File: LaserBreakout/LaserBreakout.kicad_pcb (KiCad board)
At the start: 2 copper layers, 55.9 x 34.3 mm, 7 parts, among them J1 LASER_CONN, J2 949, J3 MiniFitPower

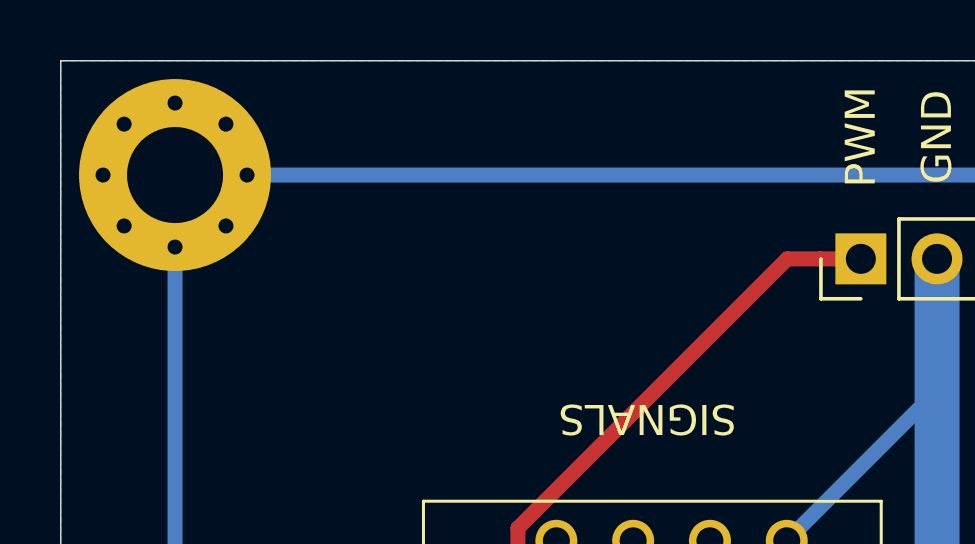
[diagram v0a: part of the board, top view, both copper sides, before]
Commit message: Add more breakout boards
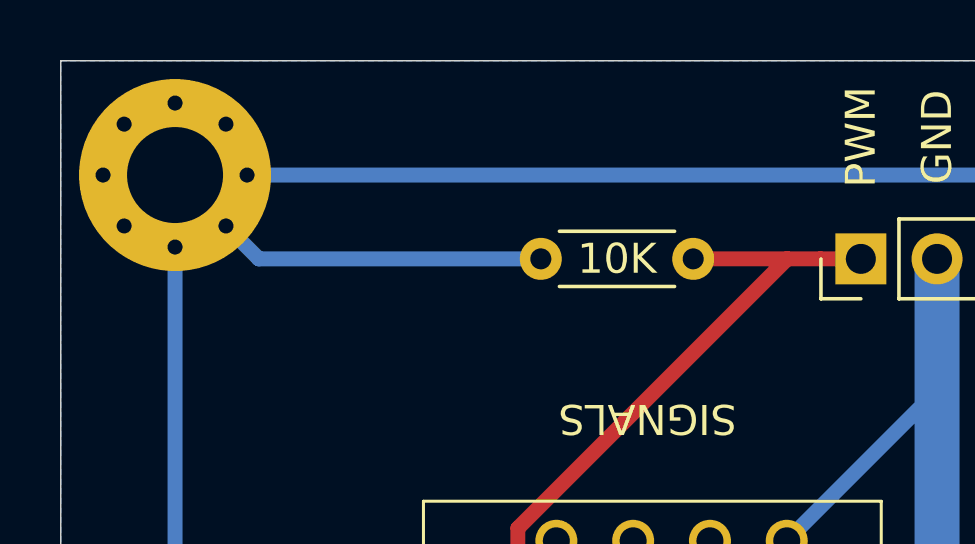
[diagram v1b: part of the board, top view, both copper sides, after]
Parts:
- added R1: 10K, Resistor_THT:R_Axial_DIN0204_L3.6mm_D1.6mm_P5.08mm_Horizontal, F.Cu at (106.2, 77.7)
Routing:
- net GND: track 204.1 -> 217.4 mm
- net 1: track 18.1 -> 21.2 mm
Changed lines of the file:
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@@
     (thickness 1.6)
     (drawings 16)
-    (tracks 21)
+    (tracks 24)
     (zones 0)
-    (modules 7)
+    (modules 8)
     (nets 12)
   )
@@
   (layers
     (0 F.Cu signal)
-    (31 B.Cu signal hide)
+    (31 B.Cu signal)
     (32 B.Adhes user)
     (33 F.Adhes user)
@@
   )
   (setup
-    (last_trace_width 1.5)
+    (last_trace_width 0.5)
     (user_trace_width 0.5)
     (user_trace_width 1)
@@
     (solder_mask_min_width 0.25)
     (aux_axis_origin 0 0)
-    (visible_elements 7FFFFFFF)
+    (visible_elements 7FFFFF7F)
     (pcbplotparams
       (layerselection 0x010fc_ffffffff)
@@
     (pad 9 thru_hole circle (at -1.235 6.35 90) (size 1.625 1.625) (drill 3.25) (layers *.Cu *.Mask F.SilkS))
     (pad 10 thru_hole circle (at 10.195 6.35 90) (size 1.625 1.625) (drill 3.25) (layers *.Cu *.Mask F.SilkS))
+    (model ${KIPRJMOD}/../libs/Keystone949/949.stp
+      (at (xyz 0 0 0))
+      (scale (xyz 1 1 1))
+      (rotate (xyz 0 0 0))
+    )
   )
   (module Connector_Molex:Molex_Mini-Fit_Jr_5566-04A_2x02_P4.20mm_Vertical (layer F.Cu)
@@
     (pad 4 thru_hole oval (at 4.2 5.5 180) (size 2.7 3.3) (drill 1.4) (layers *.Cu *.Mask)
       (net 5 24V))
-    (model ${KISYS3DMOD}/Connector_Molex.3dshapes/Molex_Mini-Fit_Jr_5566-04A_2x02_P4.20mm_Vertical.wrl
-      (at (xyz 0 0 0))
+    (model ${KIPRJMOD}/../libs/039281043.stp
+      (offset (xyz 2.1 -2.5 0))
       (scale (xyz 1 1 1))
-      (rotate (xyz 0 0 0))
+      (rotate (xyz -90 0 180))
     )
   )
@@
     )
   )
+  (module Resistor_THT:R_Axial_DIN0204_L3.6mm_D1.6mm_P5.08mm_Horizontal (layer F.Cu)
+    (at 106.172 77.724)
+    (descr "Resistor, Axial_DIN0204 series, Axial, Horizontal, pin pitch=5.08mm, 0.167W, length*diameter=3.6*1.6mm^2, http://cdn-reichelt.de/documents/datenblatt/B400/1_4W%23YAG.pdf")
+    (tags "Resistor Axial_DIN0204 series Axial Horizontal pin pitch 5.08mm 0.167W length 3.6mm diameter 1.6mm")
+    (fp_text reference R1 (at 2.54 -1.92) (layer F.SilkS) hide
+      (effects (font (size 1 1) (thickness 0.15)))
+    )
+    (fp_text value 10K (at 2.54 0) (layer F.SilkS)
+      (effects (font (size 1 1) (thickness 0.15)))
+    )
+    (fp_line (start 0.74 -0.8) (end 0.74 0.8) (layer F.Fab) (width 0.1))
+    (fp_line (start 0.74 0.8) (end 4.34 0.8) (layer F.Fab) (width 0.1))
+    (fp_line (start 4.34 0.8) (end 4.34 -0.8) (layer F.Fab) (width 0.1))
+    (fp_line (start 4.34 -0.8) (end 0.74 -0.8) (layer F.Fab) (width 0.1))
+    (fp_line (start 0 0) (end 0.74 0) (layer F.Fab) (width 0.1))
+    (fp_line (start 5.08 0) (end 4.34 0) (layer F.Fab) (width 0.1))
+    (fp_line (start 0.62 -0.92) (end 4.46 -0.92) (layer F.SilkS) (width 0.12))
+    (fp_line (start 0.62 0.92) (end 4.46 0.92) (layer F.SilkS) (width 0.12))
+    (fp_line (start -0.95 -1.05) (end -0.95 1.05) (layer F.CrtYd) (width 0.05))
+    (fp_line (start -0.95 1.05) (end 6.03 1.05) (layer F.CrtYd) (width 0.05))
+    (fp_line (start 6.03 1.05) (end 6.03 -1.05) (layer F.CrtYd) (width 0.05))
+    (fp_line (start 6.03 -1.05) (end -0.95 -1.05) (layer F.CrtYd) (width 0.05))
+    (fp_text user %R (at 2.54 0) (layer F.Fab)
+      (effects (font (size 0.72 0.72) (thickness 0.108)))
+    )
+    (pad 1 thru_hole circle (at 0 0) (size 1.4 1.4) (drill 0.7) (layers *.Cu *.Mask)
+      (net 2 GND))
+    (pad 2 thru_hole oval (at 5.08 0) (size 1.4 1.4) (drill 0.7) (layers *.Cu *.Mask)
+      (net 1 1))
+    (model ${KISYS3DMOD}/Resistor_THT.3dshapes/R_Axial_DIN0204_L3.6mm_D1.6mm_P5.08mm_Horizontal.wrl
+      (at (xyz 0 0 0))
+      (scale (xyz 1 1 1))
+      (rotate (xyz 0 0 0))
+    )
+  )
   (gr_text GND (at 119.38 73.66 90) (layer B.SilkS)
     (effects (font (size 1 1) (thickness 0.15)) (justify mirror))
@@
   (segment (start 105.41 89.662) (end 105.41 86.699998) (width 0.5) (layer F.Cu) (net 1))
   (segment (start 105.41 86.699998) (end 114.385998 77.724) (width 0.5) (layer F.Cu) (net 1))
+  (segment (start 114.385998 77.724) (end 111.252 77.724) (width 0.5) (layer F.Cu) (net 1))
   (segment (start 119.38 82.112) (end 119.38 77.724) (width 0.5) (layer B.Cu) (net 2))
   (segment (start 114.37 87.122) (end 119.38 82.112) (width 0.5) (layer B.Cu) (net 2))
@@
   (segment (start 119.38 77.724) (end 119.38 91.064705) (width 1.5) (layer B.Cu) (net 2))
   (segment (start 119.38 91.064705) (end 127.943305 99.62801) (width 1.5) (layer B.Cu) (net 2))
+  (segment (start 96.774 77.724) (end 93.98 74.93) (width 0.5) (layer B.Cu) (net 2))
+  (segment (start 106.172 77.724) (end 96.774 77.724) (width 0.5) (layer B.Cu) (net 2))
   (segment (start 121.92 78.926081) (end 121.92 77.724) (width 1.5) (layer F.Cu) (net 4))
   (segment (start 121.92 80.052) (end 121.92 78.926081) (width 1.5) (layer F.Cu) (net 4))

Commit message: So many things
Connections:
- J1 pad 1: 1 -> 2
- J2 pad 1: 1 -> Net-(J2-Pad1)
- J2 pad 2: Net-(J2-Pad2) -> 2
- R1 pad 2: 1 -> 2
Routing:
- net 1: track 21.2 -> 0.00 mm
- net 2: track 0.00 -> 16.9 mm
